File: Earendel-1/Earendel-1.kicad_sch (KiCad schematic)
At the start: 4 parts, among them U1 ATA8510-GHQW, U2 STM32F411CCUx

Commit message: Finished ATA-8510 Schem Items and filters
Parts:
- added C10, C11, C12, C2, C3, C4, C5, C6, C7, C8, C9: C, symbol Device:C
- added L2, L3: L, symbol Device:L
- added Y1: XRCGB24M000F0G00R0, XRCGB24M000F0G00R0:OSC_XRCGB24M000F0G00R0, symbol XRCGB24M000F0G00R0:XRCGB24M000F0G00R0
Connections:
- net GND: now also U1.21 (DGND), U1.30 (AGND), U1.31 (ATEST_IO2), U1.32 (ATEST_IO1), U1.9 (TEST_EN), C11.2, C12.2, C2.1, C3.2, C4.2, C5.2, C6.2, C8.2, C9.2
- net VDD: now also C5.1; no longer U1.8 (VS_PA)
- net XTAL+: now reaches U1.10 (XTAL1)
- net XTAL+: now also C11.1, Y1.1
- net XTAL-: now reaches U1.11 (XTAL2)
- net XTAL-: now also C12.1, Y1.3
- net AVCC: now reaches U1.12 (AVCC)
- net AVCC: now also C4.1
- net DVCC: now reaches U1.20 (DVCC)
- net DVCC: now also C6.1
- net CLK_OUT: now reaches U1.22 (PB0)
- net VS_TP: now reaches U1.26 (PB4)
- net SPDT_ANT: now reaches U1.4 (SPDT_ANT)
- net SPDT_ANT: now also C7.1
- net SPDT_TX: now reaches U1.6 (SPDT_TX)
- net SPDT_TX: now also C2.2, L2.1
- net RF_OUT: now reaches U1.7 (RF_OUT)
- net RF_OUT: now also L2.2
- new net: C7.2, C8.1, L3.1
- new net: C10.1, C9.1, L3.2
- new net ANT: C10.2
- new net VS_PA: C3.1, U1.8 (VS_PA)
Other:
- note added: "ATA8510 Oscillator (Note that this needs to be 24.305MHz)"
- note added: "According to datasheet this is a TP for VDD"
- note added: "CLK for the uC"
- note added: "Decoupling Caps for the ATA8510 according to the datasheets Schem"
- note added: "IMPORTANT NOTE: Pls buy the XRCGB24M305FBV1BR0, the model for the XRCGB24M000F0G00R0 is used but buy the 24.305 MHZ one please and thank you"
- note added: "Pi Filter + Coupling Caps"
- note added: "RF Matching Components"

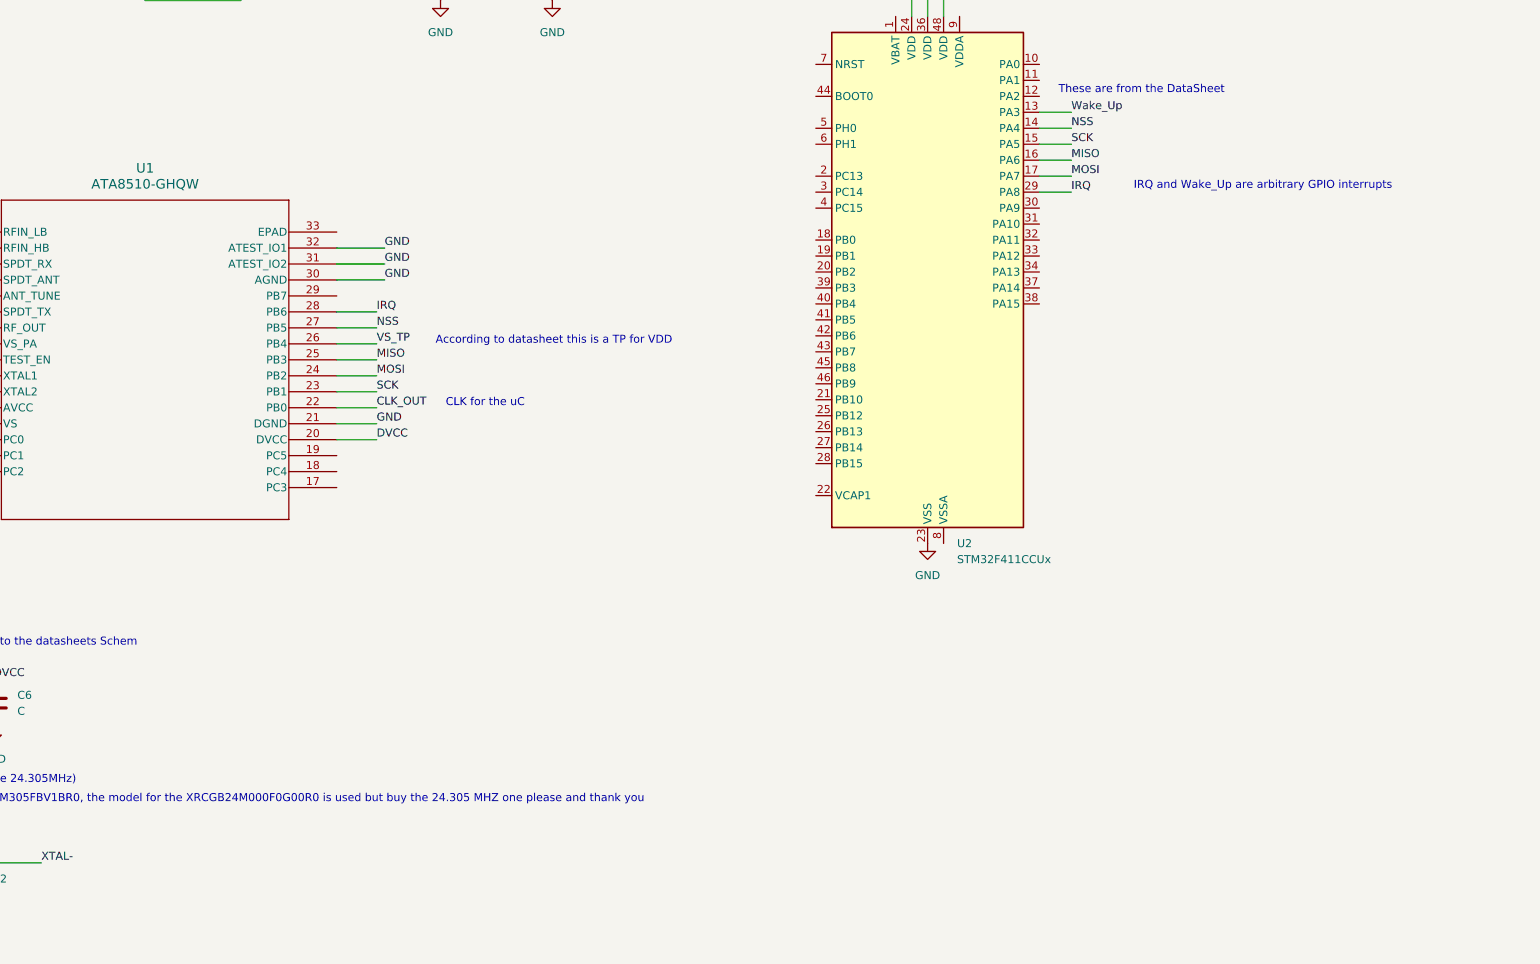
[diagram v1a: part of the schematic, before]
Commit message: JTAG header added
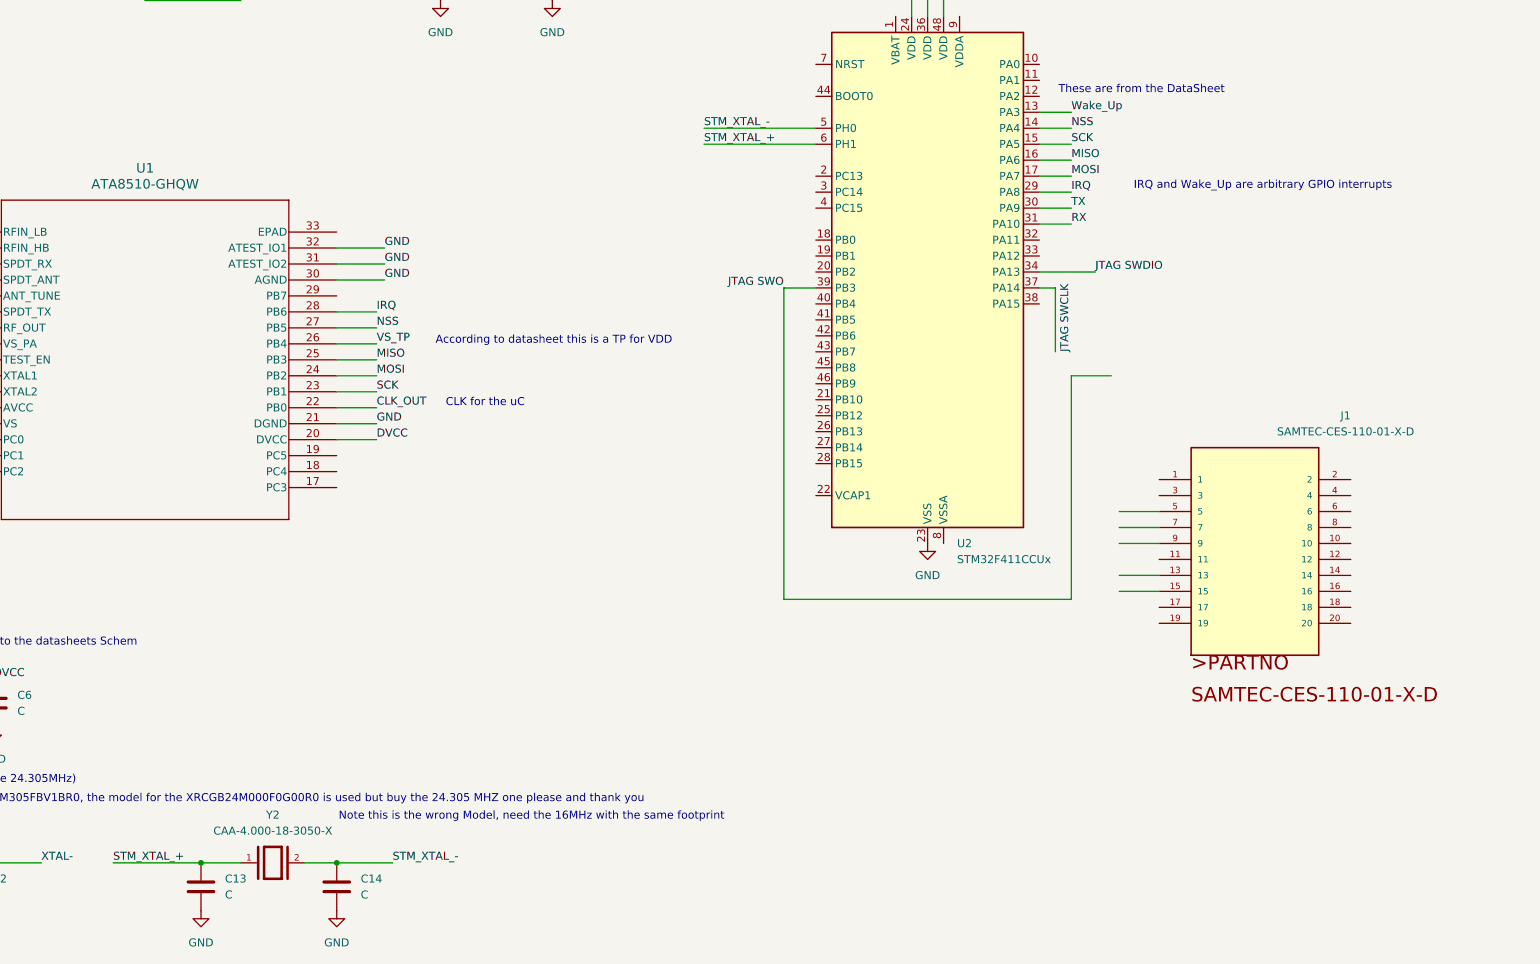
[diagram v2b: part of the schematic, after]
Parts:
- added C13, C14: C, symbol Device:C
- added J1: SAMTEC-CES-110-01-X-D, SAMTEC-CES-110-01-X-D:SAMTEC-CES-110-01-X-D, symbol SAMTEC-CES-110-01-X-D:SAMTEC-CES-110-01-X-D
- added Y2: CAA-4.000-18-3050-X, CAA-4.000-18-3050-X:XTAL_CAA-4.000-18-3050-X, symbol CAA-4.000-18-3050-X:CAA-4.000-18-3050-X
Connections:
- net GND: now also C13.2, C14.2
- net TX: now reaches U2.30 (PA9)
- net RX: now reaches U2.31 (PA10)
- net JTAG SWDIO: now reaches U2.34 (PA13)
- net STM_XTAL_-: now reaches U2.5 (PH0)
- net STM_XTAL_-: now also C14.1, Y2.2
- net STM_XTAL_+: now reaches U2.6 (PH1)
- net STM_XTAL_+: now also C13.1, Y2.1
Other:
- note added: "Note this is the wrong Model, need the 16MHz with the same footprint"

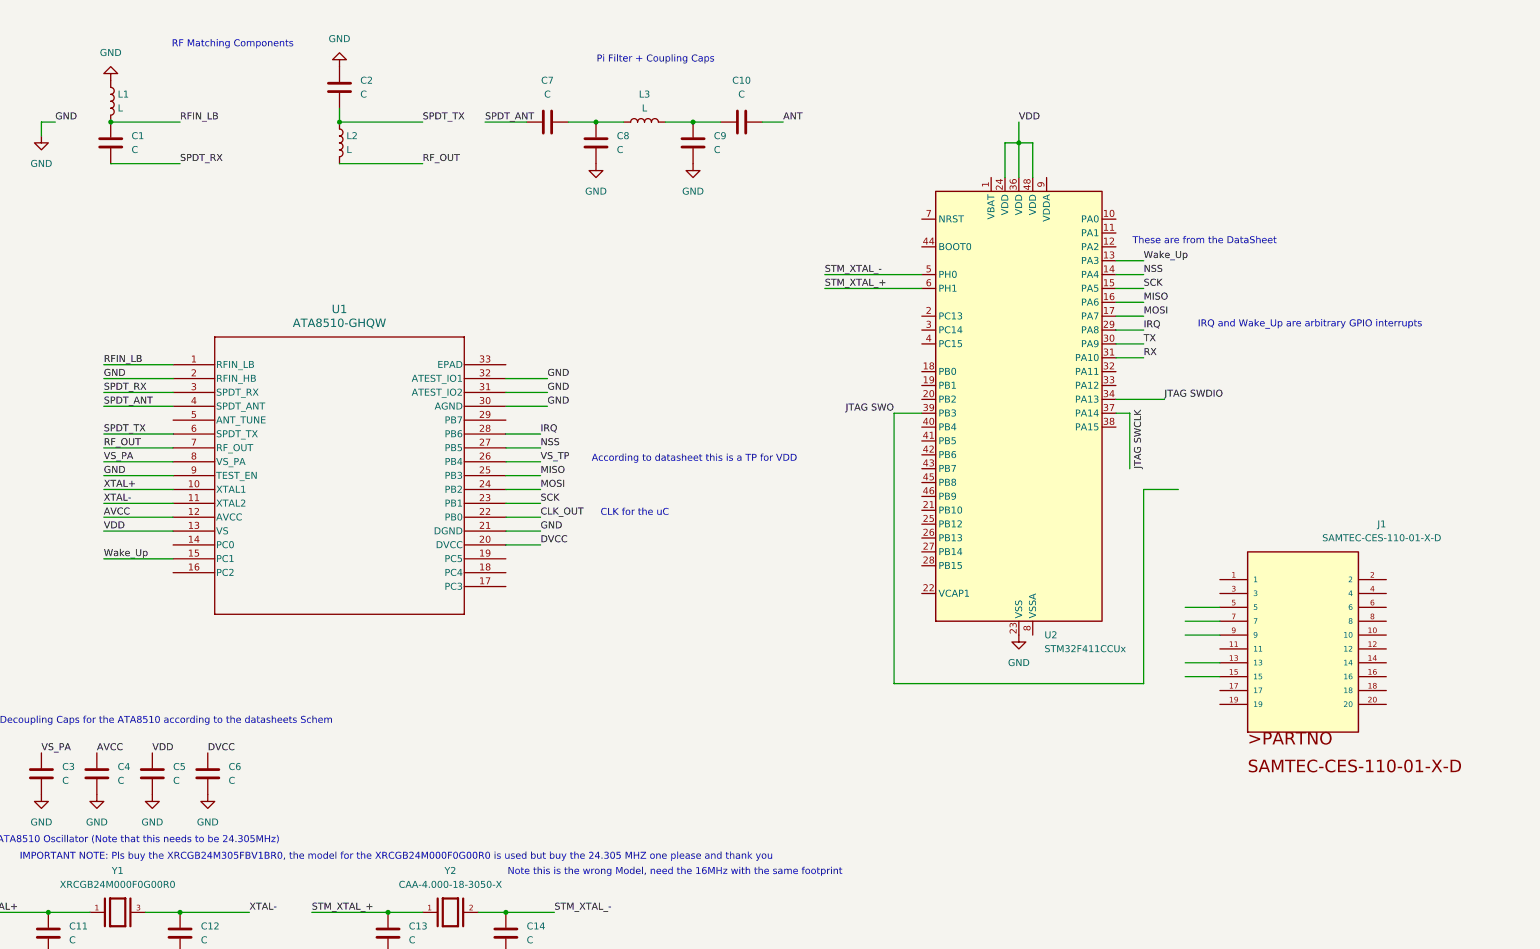
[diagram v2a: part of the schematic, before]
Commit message: UART + power headers to schematic
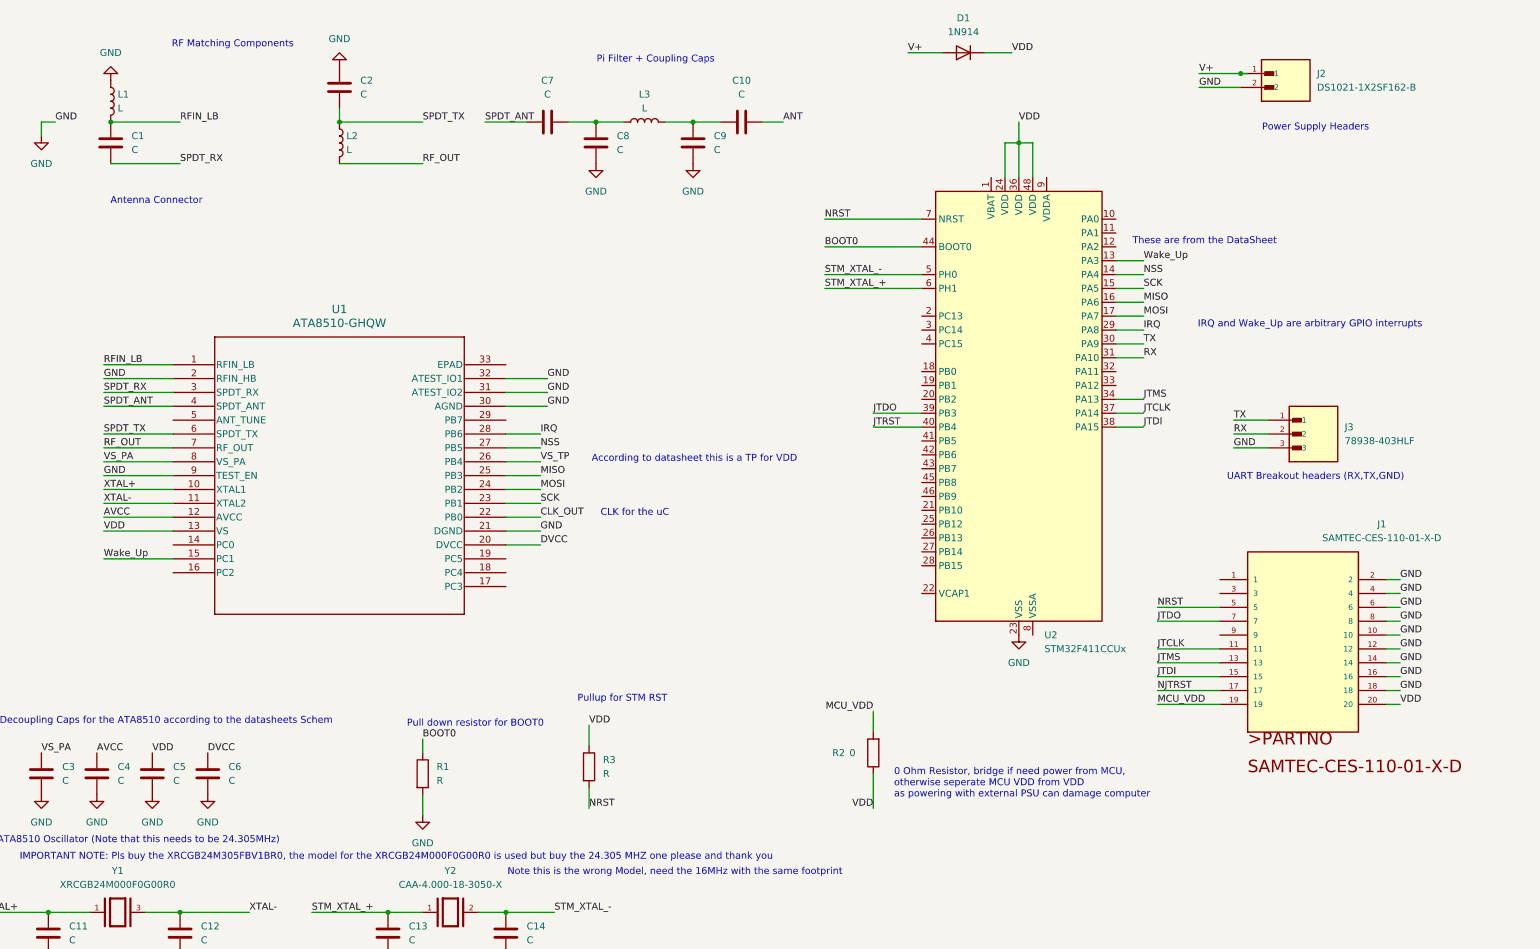
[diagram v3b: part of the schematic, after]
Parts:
- added D1: 1N914, Diode_THT:D_DO-35_SOD27_P7.62mm_Horizontal, symbol Diode:1N914
- added J2: DS1021-1X2SF162-B, DS1021-1X2SF162-B:CONNFLY_DS1021-1X2SF162-B, symbol DS1021-1X2SF162-B:DS1021-1X2SF162-B
- added J3: 78938-403HLF, 78938-403HLF:AMPHENOL_78938-403HLF, symbol 78938-403HLF:78938-403HLF
- added R1, R3: R, symbol Device:R
- added R2: 0, symbol Device:R
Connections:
- net JTAG SWDIO is gone; now on net JTMS: U2.34 (PA13)
- net GND: now also J1.10, J1.12, J1.14, J1.16, J1.18, J1.2, J1.4, J1.6, J1.8, J2.2, J3.3, R1.2
- net RX: now also J3.2
- net TX: now also J3.1
- net VDD: now also J1.20, D1.1 (K), R2.1, R3.1
- net JTCLK: now reaches U2.37 (PA14)
- net JTCLK: now also J1.11
- net JTDI: now reaches U2.38 (PA15)
- net JTDI: now also J1.15
- net JTDO: now reaches U2.39 (PB3)
- net JTDO: now also J1.7
- net JTRST: now reaches U2.40 (PB4)
- net BOOT0: now reaches U2.44 (BOOT0)
- net BOOT0: now also R1.1
- net NRST: now reaches U2.7 (NRST)
- net NRST: now also J1.5, R3.2
- net JTMS: now reaches J1.13
- net NJTRST: now reaches J1.17
- net MCU_VDD: now reaches J1.19
- net MCU_VDD: now also R2.2
- new net V+: D1.2 (A), J2.1
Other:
- note added: "0 Ohm Resistor, bridge if need power from MCU, otherwise seperate MCU VDD from VDD as powering with external PSU can damage computer"
- note added: "Antenna Connector"
- note added: "Power Supply Headers"
- note added: "Pull down resistor for BOOT0"
- note added: "Pullup for STM RST"
- note added: "UART Breakout headers (RX,TX,GND)"

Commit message: New SMA connector
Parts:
- added J4: 85_SMA-50-0-144_111_YH, 85_SMA-50-0-144_111_YH:HUBER_SUHNER_85_SMA-50-0-144_111_YH, symbol 85_SMA-50-0-144_111_YH:85_SMA-50-0-144_111_YH
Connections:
- net ANT: now also J4.1
- net GND: now also J4.G1, J4.G2, J4.G3, J4.G4
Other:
- note added: "0 Ohm resistor Bridge"
- note added: "JTAG Programming Header"
- note added: "Reverse Polarity Protection"
- note added: "SMA Connector for Antenna"
- note added: "STM32 Oscillator"
- moved on the sheet: C1, C10, C11, C12, C13, C14, C2, C7, C8, C9, D1, J1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
